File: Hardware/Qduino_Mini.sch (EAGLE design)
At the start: 39 parts, among them J1 LiPo, Q1 PFET, U1 ATMEGA32U41:1-LESS_PASTE, U2 MCP73831, U3 MAX17048, U4 AP2112K-3.3TRG-1, U5 MIGHTYQ-L-SILK, Y1 8MHZ

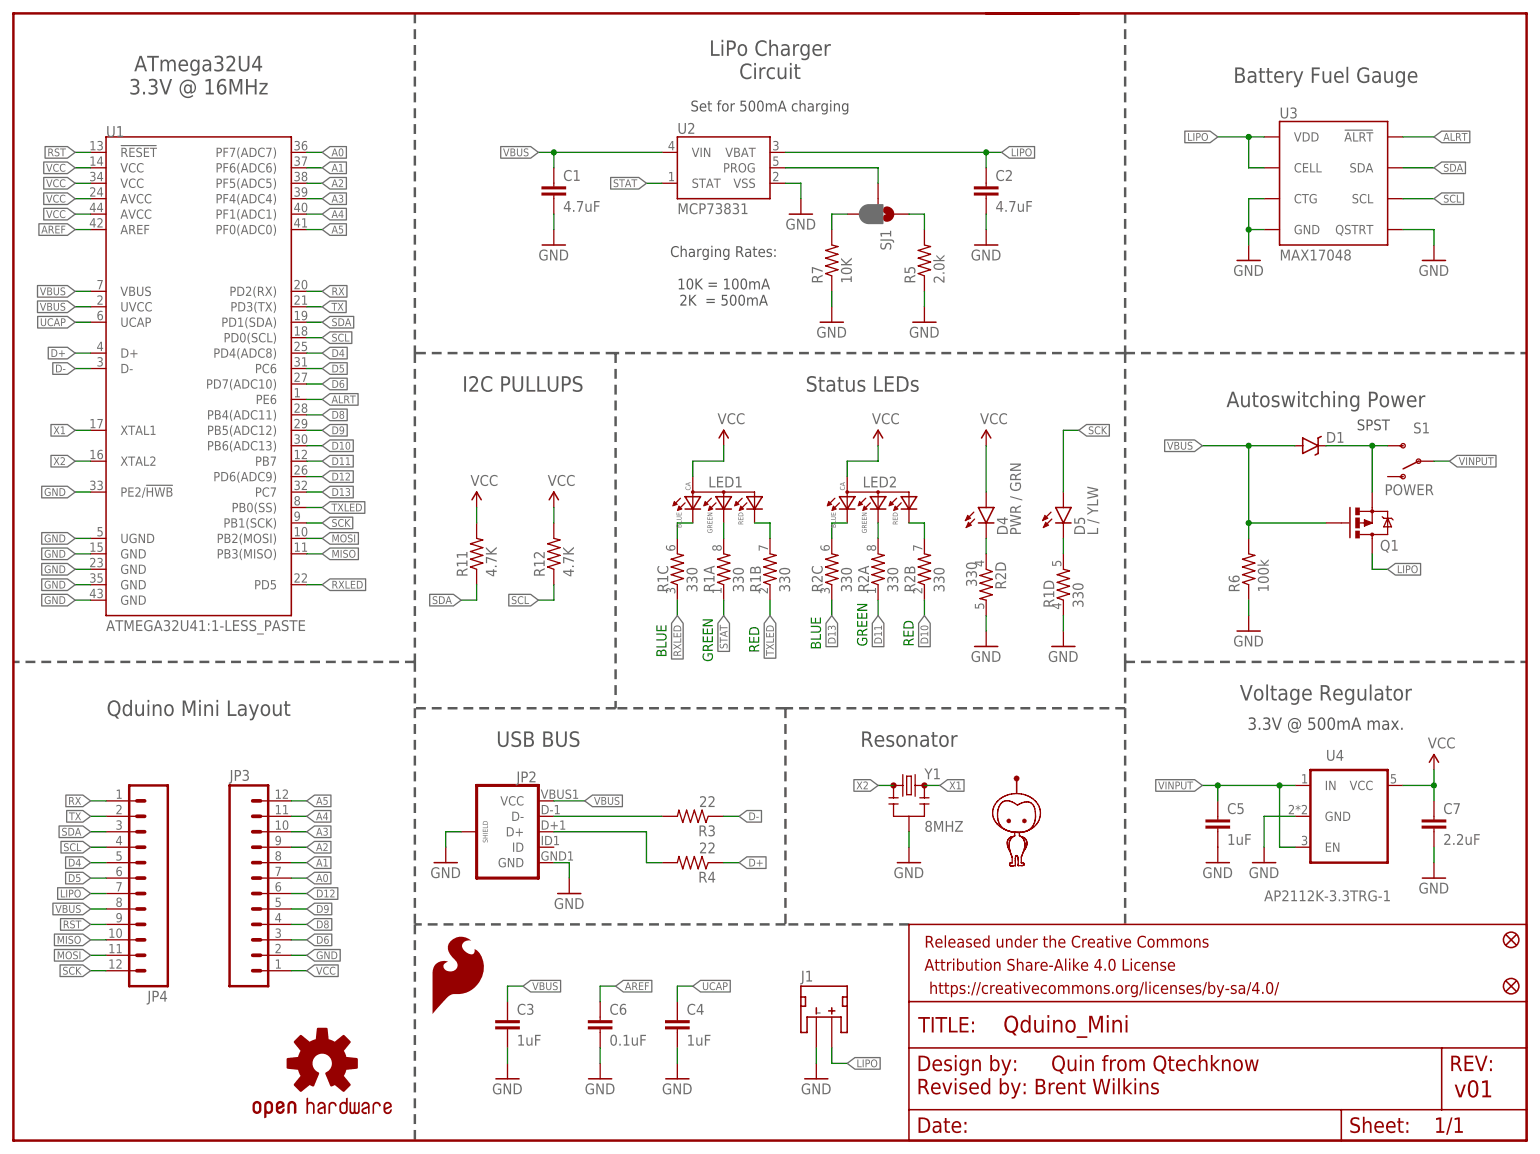
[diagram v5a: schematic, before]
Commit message: Added more ground pour, removed acid traps, cosmetic tweaks
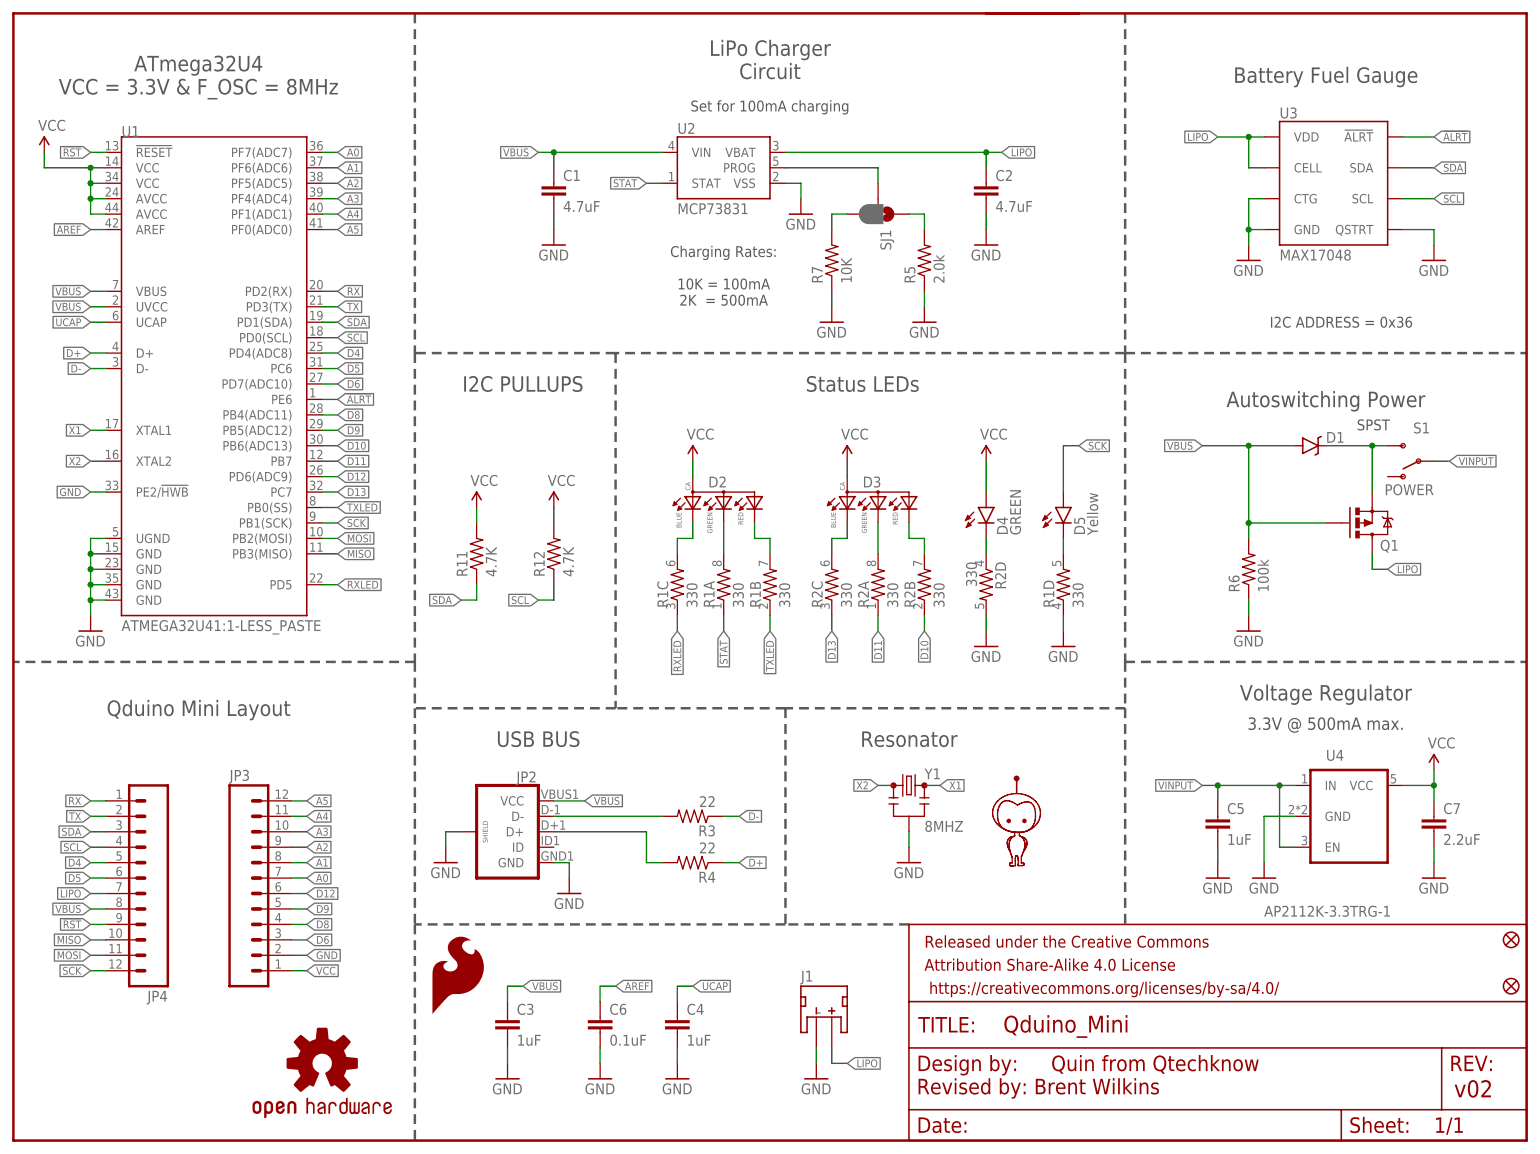
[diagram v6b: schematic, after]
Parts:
- D2, D3: PROD_ID (none) -> DIO-12986
- D4: value PWR / GRN -> GREEN
- D5: value L / YLW -> Yellow
- JP3, JP4: PROD_ID (none) -> CONN-09693
- R1, R2: PROD_ID (none) -> RES-12985
- renumbered LED1 to D2, LED2 to D3
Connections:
- net ALRT renamed !ALRT
- net RST renamed !RST
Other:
- note added: "ATmega32U4 VCC = 3.3V & F_OSC = 8MHz"
- note added: "I2C ADDRESS = 0x36"
- note added: "Set for 100mA charging"
- note removed: "ATmega32U4 3.3V @ 16MHz"
- note removed: "BLUE"
- note removed: "GREEN"
- note removed: "RED"
- note removed: "Set for 500mA charging"
- moved on the sheet: R1A, R1B, R1C, R2A, R2B, R2C, U1

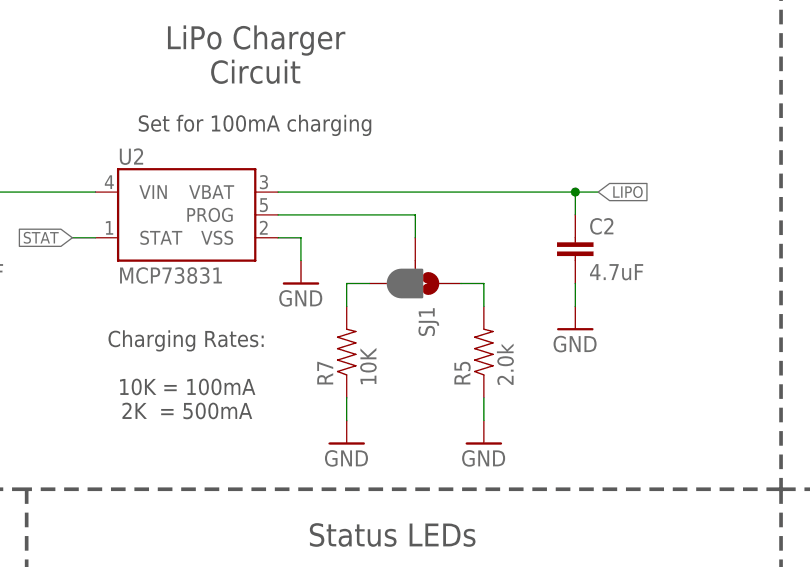
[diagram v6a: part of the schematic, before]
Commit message: internally connected solder jumper, moved traces around new vias on USB
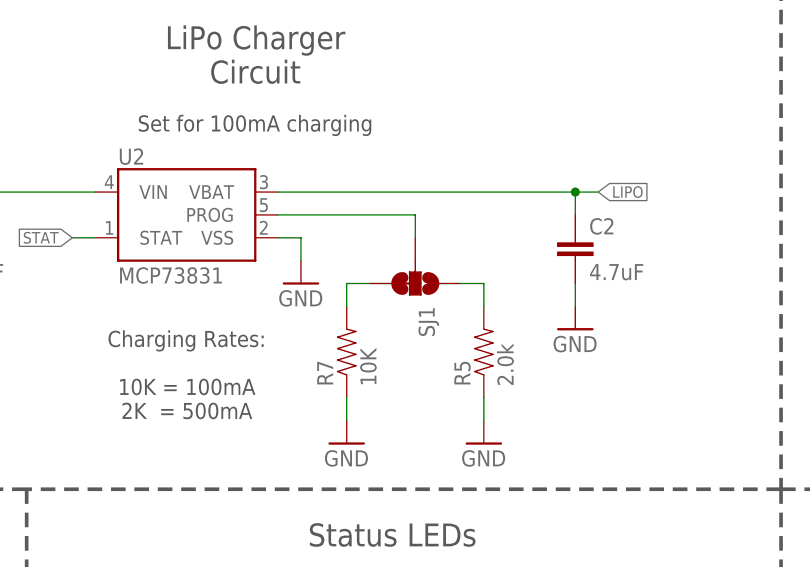
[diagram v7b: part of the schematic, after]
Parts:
- SJ1: value JUMPER-PAD-3-2OF3_NC_BY_PASTE -> JUMPER-PAD-3-2OF3_NC_BY_TRACE_SMALL; device SparkFun-Passives:JUMPER-PAD-3-2OF3_NC_BY_PASTE -> SparkFun-Passives:JUMPER-PAD-3-2OF3_NC_BY_TRACE_SMALL
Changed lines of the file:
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@@
 <?xml version="1.0" encoding="utf-8"?>
 <!DOCTYPE eagle SYSTEM "eagle.dtd">
-<eagle version="7.2.0">
+<eagle version="7.1.0">
 <drawing>
 <settings>
@@
 <part name="D1" library="SparkFun-DiscreteSemi" deviceset="DIODE-SCHOTTKY" device="-BAT20J" value="BAT20J"/>
 <part name="U5" library="SparkFun-Aesthetics" deviceset="MIGHTYQ-L-SILK" device=""/>
-<part name="SJ1" library="SparkFun-Passives" deviceset="JUMPER-PAD-3-2OF3_NC_BY_PASTE" device="" value=""/>
 <part name="GND8" library="SparkFun" deviceset="GND" device=""/>
 <part name="R7" library="SparkFun-Resistors" deviceset="10KOHM-1/10W-1%(0603)" device="0603" value="10K"/>
@@
 <part name="GND4" library="SparkFun" deviceset="GND" device=""/>
 <part name="P+1" library="SFE Aesthetics" deviceset="VCC" device=""/>
+<part name="SJ1" library="SparkFun-Passives" deviceset="JUMPER-PAD-3-2OF3_NC_BY_TRACE" device="_SMALL" value=""/>
 </parts>
 <sheets>
@@
 </instance>
 <instance part="U5" gate="G$1" x="78.74" y="0"/>
-<instance part="SJ1" gate="G$1" x="55.88" y="101.6" rot="R270"/>
 <instance part="GND8" gate="1" x="48.26" y="83.82"/>
 <instance part="R7" gate="G$1" x="48.26" y="93.98" rot="R90"/>
@@
 <instance part="GND4" gate="1" x="-73.66" y="33.02"/>
 <instance part="P+1" gate="1" x="-81.28" y="111.76"/>
+<instance part="SJ1" gate="G$1" x="55.88" y="101.6" rot="R270"/>
 </instances>
 <busses>
@@
 <wire x1="40.64" y1="109.22" x2="55.88" y2="109.22" width="0.1524" layer="91"/>
 <pinref part="U2" gate="G$1" pin="PROG"/>
+<wire x1="55.88" y1="109.22" x2="55.88" y2="106.68" width="0.1524" layer="91"/>
 <pinref part="SJ1" gate="G$1" pin="2"/>
-<wire x1="55.88" y1="109.22" x2="55.88" y2="106.68" width="0.1524" layer="91"/>
 </segment>
 </net>
@@
 <net name="N$6" class="0">
 <segment>
-<pinref part="SJ1" gate="G$1" pin="3"/>
 <pinref part="R7" gate="G$1" pin="2"/>
 <wire x1="50.8" y1="101.6" x2="48.26" y2="101.6" width="0.1524" layer="91"/>
 <wire x1="48.26" y1="101.6" x2="48.26" y2="99.06" width="0.1524" layer="91"/>
+<pinref part="SJ1" gate="G$1" pin="3"/>
 </segment>
 </net>
 <net name="N$7" class="0">
 <segment>
-<pinref part="SJ1" gate="G$1" pin="1"/>
 <pinref part="R5" gate="G$1" pin="2"/>
 <wire x1="60.96" y1="101.6" x2="63.5" y2="101.6" width="0.1524" layer="91"/>
 <wire x1="63.5" y1="101.6" x2="63.5" y2="99.06" width="0.1524" layer="91"/>
-</segment>
-</net>
+<pinref part="SJ1" gate="G$1" pin="1"/>
+</segment>
+</net>

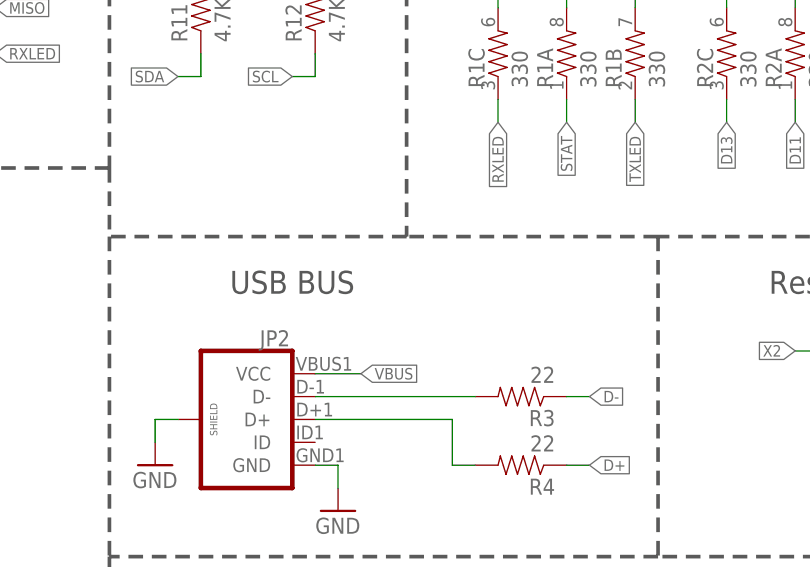
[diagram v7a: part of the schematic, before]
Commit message: Added note to follow USB spec for USB port
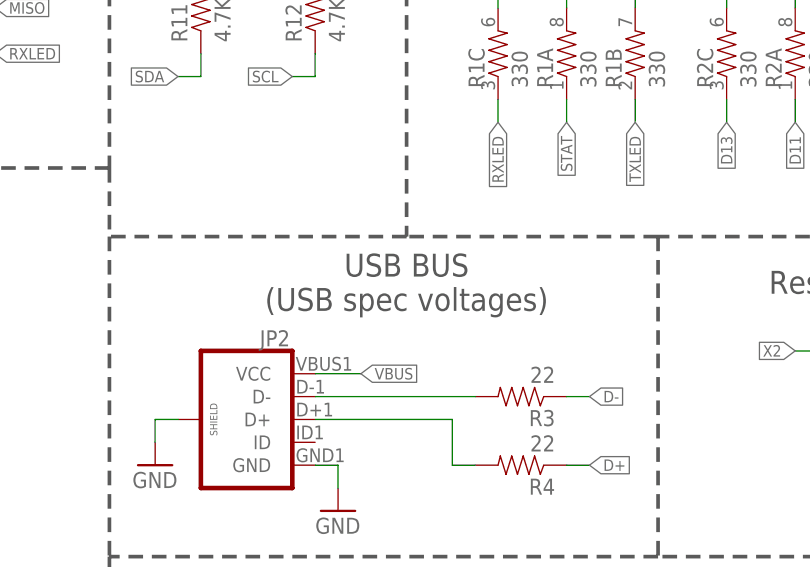
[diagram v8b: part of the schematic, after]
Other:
- note added: "USB BUS (USB spec voltages)"
- note removed: "USB BUS"
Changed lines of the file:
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@@
 <?xml version="1.0" encoding="utf-8"?>
 <!DOCTYPE eagle SYSTEM "eagle.dtd">
-<eagle version="7.1.0">
+<eagle version="7.2.0">
 <drawing>
 <settings>
@@
 <plain>
 <text x="38.1" y="119.38" size="1.778" layer="97" align="center">Set for 100mA charging</text>
-<text x="0" y="15.24" size="2.54" layer="97" align="center">USB BUS</text>
+<text x="12.7" y="15.24" size="2.54" layer="97" font="vector" align="center">USB BUS
+(USB spec voltages)</text>
 <text x="60.96" y="15.24" size="2.54" layer="97" align="center">Resonator</text>
 <text x="53.34" y="73.66" size="2.54" layer="97" align="center">Status LEDs</text>
